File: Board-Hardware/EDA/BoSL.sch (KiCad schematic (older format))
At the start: 56 parts, among them CON1 Micro_SD_Card, CON2 BARREL_JACK, IC1 ATMEGA328-P, IC2 SIM7000, J1 Screw_Terminal_1x06, J2 Screw_Terminal_1x04, J3 Screw_Terminal_1x02, J4 Screw_Terminal_1x08, J5 Screw_Terminal_1x04, J6 RJ45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

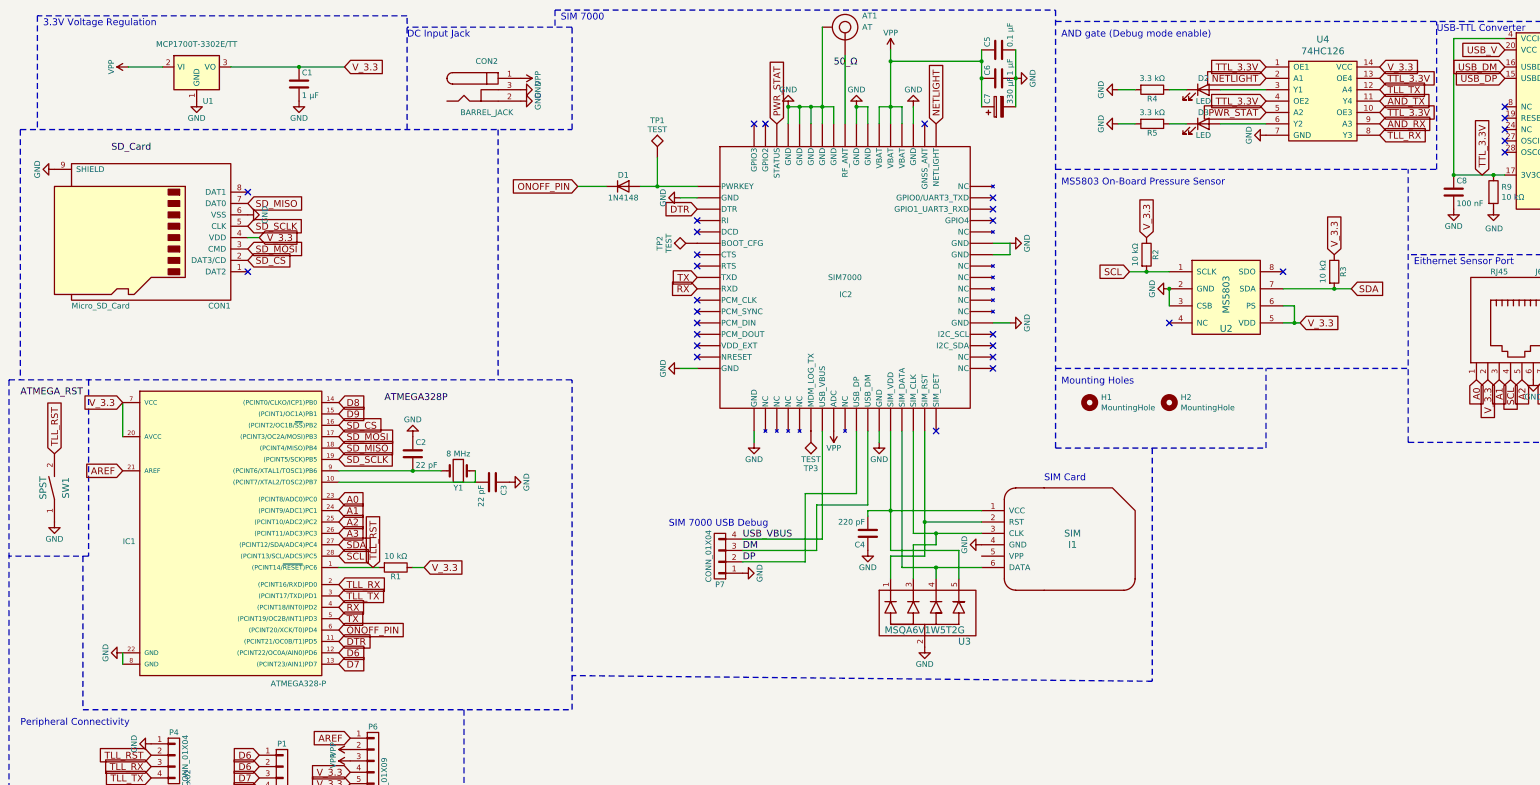
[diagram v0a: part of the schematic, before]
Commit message: renamed bosl GPS to bosl
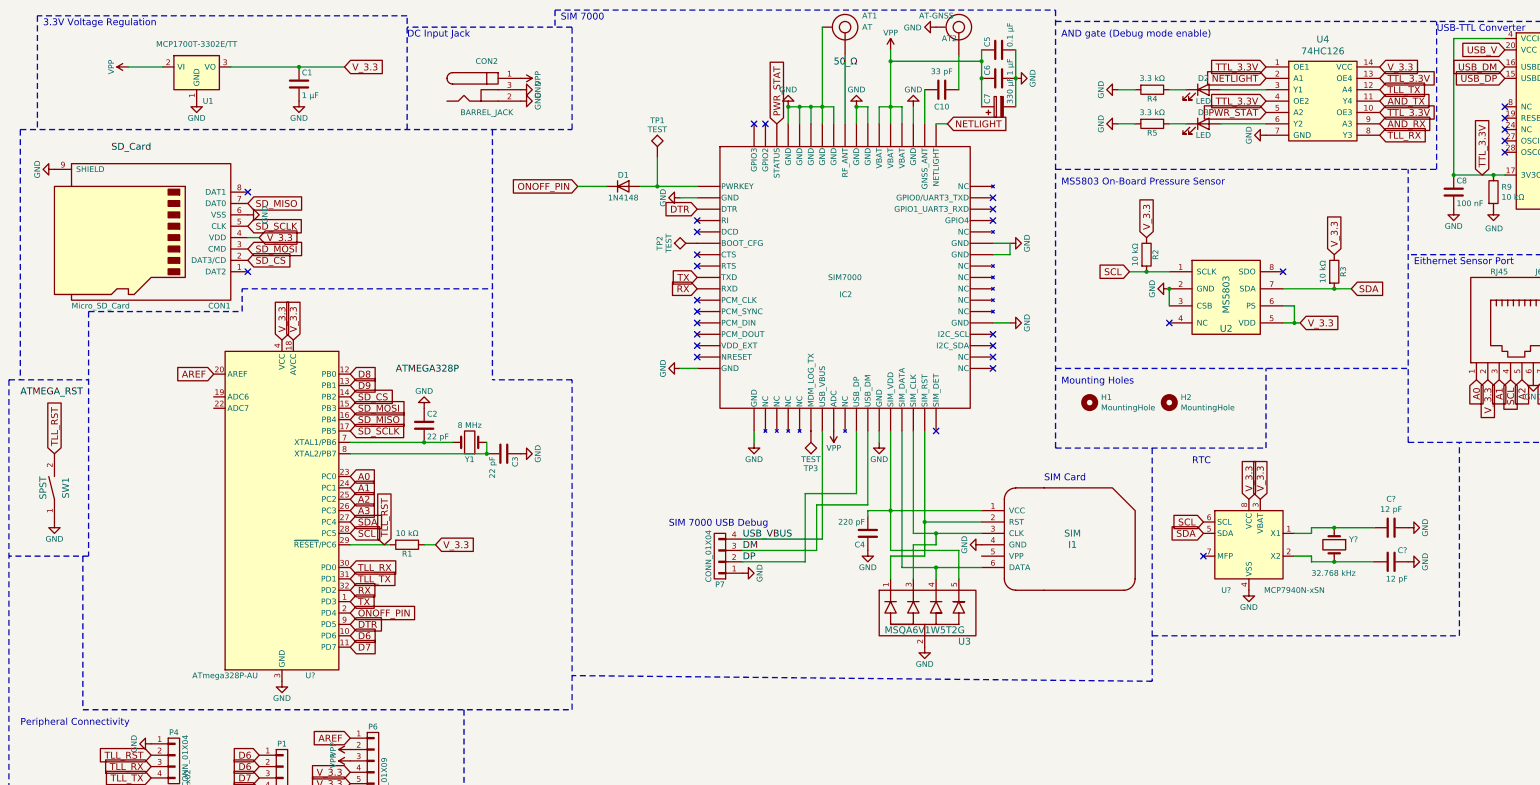
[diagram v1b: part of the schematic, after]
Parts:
- removed IC1: ATMEGA328-P, Housings_DIP:DIP-28_W7.62mm_Socket_LongPads, symbol SIM7000-rescue:ATMEGA328-P-SIM7000-rescue
- added AT2: AT-GNSS, Connectors_Molex:Molex_Microcoaxial_RF, symbol SIM7000-rescue:AT-ant
- added C10: 33 pF, Capacitors_SMD:C_0805_HandSoldering, symbol Device:C
- added C? (x2): 12 pF, Capacitor_SMD:C_0805_2012Metric, symbol Device:C
- added U?: MCP7940N-xSN, symbol Timer:MCP7940N-xSN
- added U?: ATmega328P-AU, Package_QFP:TQFP-32_7x7mm_P0.8mm, symbol MCU_Microchip_ATmega:ATmega328P-AU
- added Y?: 32.768 kHz, Crystal:Crystal_SMD_EuroQuartz_EQ161-2Pin_3.2x1.5mm, symbol Device:Crystal
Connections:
- net A0: now also U?.23 (PC0)
- net A1: now also U?.24 (PC1)
- net A2: now also U?.25 (PC2)
- net A3: now also U?.26 (PC3)
- net AREF: now also U?.20 (AREF)
- net D6: now also U?.10 (PD6)
- net D7: now also U?.11 (PD7)
- net D8: now also U?.12 (PB0)
- net D9: now also U?.13 (PB1)
- net DTR: now also U?.9 (PD5)
- net GND: now also AT2.2, C?.1, C?.1, U?.21 (GND), U?.3 (GND), U?.4 (VSS), U?.5 (GND)
- net ONOFF_PIN: now also U?.2 (PD4)
- net RX: now also U?.32 (PD2)
- net SCL: now also U?.28 (PC5), U?.6 (SCL)
- net SDA: now also U?.27 (PC4), U?.5 (SDA)
- net SD_CS: now also U?.14 (PB2)
- net SD_MISO: now also U?.16 (PB4)
- net SD_MOSI: now also U?.15 (PB3)
- net SD_SCLK: now also U?.17 (PB5)
- net TLL_RST: now also U?.29 (~RESET~/PC6)
- net TLL_RX: now also U?.30 (PD0)
- net TLL_TX: now also U?.31 (PD1)
- net TX: now also U?.1 (PD3)
- net V_3.3: now also U?.18 (AVCC), U?.3 (VBAT), U?.4 (VCC), U?.6 (VCC), U?.8 (VCC)
- net at IC2.53 (GNSS_ANT): now also C10.2
- net at C3.2, Y1.1: now also U?.8 (XTAL2/PB7)
- net at C2.2, Y1.2: now also U?.7 (XTAL1/PB6)
- new net: AT2.1, C10.1
- new net: C?.2, U?.1 (X1), Y?.1
- new net: C?.2, U?.2 (X2), Y?.2
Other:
- note added: "RTC\n"
- moved on the sheet: C2, C3, R1, Y1

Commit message: begun layout of bosl board rev 0.4
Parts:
- U7: renamed from U?; footprint (none) -> Package_SO:SOIC-8_3.9x4.9mm_P1.27mm
- gave numbers to parts that had none: 4
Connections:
- net D6: now also J4.3, P1.5 (P5), P1.6 (P6); no longer J4.1, P1.1 (P1), P1.2 (P2)
- net D7: now also J4.4, P1.7 (P7), P1.8 (P8); no longer J4.2, P1.3 (P3), P1.4 (P4)
- net RX: now also U6.12 (PB0); no longer U6.32 (PD2)
- net TX: now also U6.13 (PB1); no longer U6.1 (PD3)
- removed net D8: J4.3, P1.5 (P5), P1.6 (P6), U6.12 (PB0)
- removed net D9: J4.4, P1.7 (P7), P1.8 (P8), U6.13 (PB1)
- new net D2: J4.1, P1.1 (P1), P1.2 (P2), U6.32 (PD2)
- new net D3: J4.2, P1.3 (P3), P1.4 (P4), U6.1 (PD3)
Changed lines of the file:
@@
 	0    -1   -1   0
 $EndComp
-Text GLabel 3500 3800 2    60   Input ~ 0
-D9
+Text GLabel 3500 5700 2    60   Input ~ 0
+D3
 $Comp
 L power:VPP #PWR04
@@
 Text GLabel 3500 4200 2    60   Input ~ 0
 SD_SCLK
-Text GLabel 3500 5600 2    60   Input ~ 0
+Text GLabel 3500 3700 2    60   Input ~ 0
 RX
-Text GLabel 3500 5700 2    60   Input ~ 0
+Text GLabel 3500 3800 2    60   Input ~ 0
 TX
 Text GLabel 3500 4000 2    60   Input ~ 0
@@
 Text GLabel 3500 6100 2    60   Input ~ 0
 D7
-Text GLabel 3500 3700 2    60   Input ~ 0
-D8
+Text GLabel 3500 5600 2    60   Input ~ 0
+D2
 Text GLabel 2300 3700 0    60   Input ~ 0
 AREF
@@
 Text GLabel 2800 9400 0    60   Input ~ 0
 SD_CS
+Text GLabel 2800 10000 0    60   Input ~ 0
+D3
+Text GLabel 2800 10200 0    60   Input ~ 0
+D2
 Text GLabel 2800 9600 0    60   Input ~ 0
-D9
-Text GLabel 2800 9800 0    60   Input ~ 0
-D8
-Text GLabel 2800 10000 0    60   Input ~ 0
 D7
 $Comp
@@
 	-1   0    0    1
 $EndComp
-Text GLabel 2800 10200 0    60   Input ~ 0
+Text GLabel 2800 9800 0    60   Input ~ 0
 D6
 $Comp
@@
 	1    0    0    -1
 $EndComp
+Text GLabel 2700 7450 0    60   Input ~ 0
+D6
+Text GLabel 2700 7550 0    60   Input ~ 0
+D6
+Text GLabel 2700 7650 0    60   Input ~ 0
+D7
+Text GLabel 2700 7750 0    60   Input ~ 0
+D7
 Text GLabel 2700 7050 0    60   Input ~ 0
-D6
+D2
 Text GLabel 2700 7150 0    60   Input ~ 0
-D6
+D2
 Text GLabel 2700 7250 0    60   Input ~ 0
-D7
+D3
 Text GLabel 2700 7350 0    60   Input ~ 0
-D7
-Text GLabel 2700 7450 0    60   Input ~ 0
-D8
-Text GLabel 2700 7550 0    60   Input ~ 0
-D8
-Text GLabel 2700 7650 0    60   Input ~ 0
-D9
-Text GLabel 2700 7750 0    60   Input ~ 0
-D9
+D3
 Text GLabel 2700 7850 0    60   Input ~ 0
 SD_CS
@@
 $EndComp
 $Comp
-L Timer:MCP7940N-xSN U?
+L Timer:MCP7940N-xSN U7
 U 1 1 5E98247E
 P 11400 5200
-F 0 "U?" H 11200 4800 50  0000 C CNN
+F 0 "U7" H 11200 4800 50  0000 C CNN
 F 1 "MCP7940N-xSN" H 11800 4800 50  0000 C CNN
-F 2 "" H 11400 5200 50  0001 C CNN
+F 2 "Package_SO:SOIC-8_3.9x4.9mm_P1.27mm" H 11400 5200 50  0001 C CNN
 F 3 "http://ww1.microchip.com/downloads/en/DeviceDoc/20005010F.pdf" H 11400 5200 50  0001 C CNN
 	1    11400 5200
@@
 V_3.3
 $Comp
-L power:GND #PWR?
+L power:GND #PWR022
 U 1 1 5E98293F
 P 11400 5600
-F 0 "#PWR?" H 11400 5350 50  0001 C CNN
+F 0 "#PWR022" H 11400 5350 50  0001 C CNN
 F 1 "GND" H 11400 5450 50  0000 C CNN
 F 2 "" H 11400 5600 50  0000 C CNN
@@
 $EndComp
 $Comp
-L Device:Crystal Y?
+L Device:Crystal Y2
 U 1 1 5E983AB6
 P 12150 5200
-F 0 "Y?" V 12104 5331 50  0000 L CNN
+F 0 "Y2" V 12104 5331 50  0000 L CNN
 F 1 " 32.768 kHz" V 12400 5000 50  0000 L CNN
 F 2 "Crystal:Crystal_SMD_EuroQuartz_EQ161-2Pin_3.2x1.5mm" H 12150 5200 50  0001 C CNN
@@
 $EndComp
 $Comp
-L Device:C C?
+L Device:C C11
 U 1 1 5E983D64
 P 12650 5050
-F 0 "C?" V 12398 5050 50  0000 C CNN
+F 0 "C11" V 12398 5050 50  0000 C CNN
 F 1 "12 pF" V 12489 5050 50  0000 C CNN
 F 2 "Capacitor_SMD:C_0805_2012Metric" H 12688 4900 50  0001 C CNN
@@
 $EndComp
 $Comp
-L Device:C C?
+L Device:C C12
 U 1 1 5E984B65
 P 12650 5350
-F 0 "C?" V 12550 5450 50  0000 C CNN
+F 0 "C12" V 12550 5500 50  0000 C CNN
 F 1 "12 pF" V 12800 5400 50  0000 C CNN
 F 2 "Capacitor_SMD:C_0805_2012Metric" H 12688 5200 50  0001 C CNN
@@
 	12150 5350 11950 5350
 $Comp
-L power:GND #PWR?
+L power:GND #PWR053
 U 1 1 5E990792
 P 12800 5050
-F 0 "#PWR?" H 12800 4800 50  0001 C CNN
+F 0 "#PWR053" H 12800 4800 50  0001 C CNN
 F 1 "GND" H 12800 4900 50  0000 C CNN
 F 2 "" H 12800 5050 50  0000 C CNN
@@
 $EndComp
 $Comp
-L power:GND #PWR?
+L power:GND #PWR054
 U 1 1 5E990C8E
 P 12800 5350
-F 0 "#PWR?" H 12800 5100 50  0001 C CNN
+F 0 "#PWR054" H 12800 5100 50  0001 C CNN
 F 1 "GND" H 12800 5200 50  0000 C CNN
 F 2 "" H 12800 5350 50  0000 C CNN
@@
 RTC\n
 $Comp
-L MCU_Microchip_ATmega:ATmega328P-AU U?
+L MCU_Microchip_ATmega:ATmega328P-AU U6
 U 1 1 5E998630
 P 2900 4900
-F 0 "U?" H 3150 3450 50  0000 C CNN
+F 0 "U6" H 3150 3450 50  0000 C CNN
 F 1 "ATmega328P-AU" H 2400 3450 50  0000 C CNN
 F 2 "Package_QFP:TQFP-32_7x7mm_P0.8mm" H 2900 4900 50  0001 C CIN

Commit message: finished bosl board rev0.4 layout
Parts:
- C1, C6: footprint Capacitors_SMD:C_1206_HandSoldering -> Capacitor_SMD:C_1206_3216Metric
- C10, C2, C3, C4, C5, C8, C9: footprint Capacitors_SMD:C_0805_HandSoldering -> Capacitor_SMD:C_0805_2012Metric
- D2, D3, D4, D5, D6: footprint LEDs:LED_0805_HandSoldering -> LED_SMD:LED_0805_2012Metric
- R1, R2, R3, R4, R5, R6, R7, R8, R9: footprint Resistors_SMD:R_0805_HandSoldering -> Resistor_SMD:R_0805_2012Metric
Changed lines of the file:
@@
 F 0 "R1" V 4080 5200 50  0000 C CNN
 F 1 "10 kΩ" V 3900 5200 50  0000 C CNN
-F 2 "Resistors_SMD:R_0805_HandSoldering" V 3930 5200 50  0001 C CNN
+F 2 "Resistor_SMD:R_0805_2012Metric" V 3930 5200 50  0001 C CNN
 F 3 "" H 4000 5200 50  0000 C CNN
 	1    4000 5200
@@
 F 0 "C2" H 4175 4250 50  0000 L CNN
 F 1 "22 pF" H 4175 4050 50  0000 L CNN
-F 2 "Capacitors_SMD:C_0805_HandSoldering" H 4188 4000 50  0001 C CNN
+F 2 "Capacitor_SMD:C_0805_2012Metric" H 4188 4000 50  0001 C CNN
 F 3 "" H 4150 4150 50  0000 C CNN
 	1    4150 4150
@@
 F 0 "C3" H 4875 4500 50  0000 L CNN
 F 1 "22 pF" H 4875 4300 50  0000 L CNN
-F 2 "Capacitors_SMD:C_0805_HandSoldering" H 4888 4250 50  0001 C CNN
+F 2 "Capacitor_SMD:C_0805_2012Metric" H 4888 4250 50  0001 C CNN
 F 3 "" H 4850 4400 50  0000 C CNN
 	1    4850 4400
@@
 F 0 "C4" H 8075 5200 50  0000 L CNN
 F 1 "220 pF" H 8075 5000 50  0000 L CNN
-F 2 "Capacitors_SMD:C_0805_HandSoldering" H 8088 4950 50  0001 C CNN
+F 2 "Capacitor_SMD:C_0805_2012Metric" H 8088 4950 50  0001 C CNN
 F 3 "" H 8050 5100 50  0000 C CNN
 	1    8050 5100
@@
 F 0 "C1" H 3075 1250 50  0000 L CNN
 F 1 "1 μF" H 3075 1050 50  0000 L CNN
-F 2 "Capacitors_SMD:C_1206_HandSoldering" H 3088 1000 50  0001 C CNN
+F 2 "Capacitor_SMD:C_1206_3216Metric" H 3088 1000 50  0001 C CNN
 F 3 "" H 3050 1150 50  0000 C CNN
 	1    3050 1150
@@
 F 0 "C5" H 9225 950 50  0000 L CNN
 F 1 "0.1 μF" H 9225 750 50  0000 L CNN
-F 2 "Capacitors_SMD:C_0805_HandSoldering" H 9238 700 50  0001 C CNN
+F 2 "Capacitor_SMD:C_0805_2012Metric" H 9238 700 50  0001 C CNN
 F 3 "" H 9200 850 50  0000 C CNN
 	1    9200 850
@@
 F 0 "C6" H 9225 1200 50  0000 L CNN
 F 1 "1 μF" H 9225 1000 50  0000 L CNN
-F 2 "Capacitors_SMD:C_1206_HandSoldering" H 9238 950 50  0001 C CNN
+F 2 "Capacitor_SMD:C_1206_3216Metric" H 9238 950 50  0001 C CNN
 F 3 "" H 9200 1100 50  0000 C CNN
 	1    9200 1100
@@
 F 0 "C8" H 13225 2200 50  0000 L CNN
 F 1 "100 nF" H 13225 2000 50  0000 L CNN
-F 2 "Capacitors_SMD:C_0805_HandSoldering" H 13238 1950 50  0001 C CNN
+F 2 "Capacitor_SMD:C_0805_2012Metric" H 13238 1950 50  0001 C CNN
 F 3 "" H 13200 2100 50  0000 C CNN
 	1    13200 2100
@@
 F 0 "C9" H 15125 1250 50  0000 L CNN
 F 1 "100 nF" H 15125 1050 50  0000 L CNN
-F 2 "Capacitors_SMD:C_0805_HandSoldering" H 15138 1000 50  0001 C CNN
+F 2 "Capacitor_SMD:C_0805_2012Metric" H 15138 1000 50  0001 C CNN
 F 3 "" H 15100 1150 50  0000 C CNN
 	1    15100 1150
@@
 F 0 "D5" H 15450 1650 50  0000 C CNN
 F 1 "LED" H 15450 1450 50  0000 C CNN
-F 2 "LEDs:LED_0805_HandSoldering" H 15450 1550 50  0001 C CNN
+F 2 "LED_SMD:LED_0805_2012Metric" H 15450 1550 50  0001 C CNN
 F 3 "" H 15450 1550 50  0000 C CNN
 	1    15450 1550
@@
 F 0 "R7" V 15180 1550 50  0000 C CNN
 F 1 "3.3 kΩ" V 15000 1550 50  0000 C CNN
-F 2 "Resistors_SMD:R_0805_HandSoldering" V 15030 1550 50  0001 C CNN
+F 2 "Resistor_SMD:R_0805_2012Metric" V 15030 1550 50  0001 C CNN
 F 3 "" H 15100 1550 50  0000 C CNN
 	1    15100 1550
@@
 F 0 "D4" H 15750 3700 50  0000 C CNN
 F 1 "LED" H 15750 3500 50  0000 C CNN
-F 2 "LEDs:LED_0805_HandSoldering" H 15750 3600 50  0001 C CNN
+F 2 "LED_SMD:LED_0805_2012Metric" H 15750 3600 50  0001 C CNN
 F 3 "" H 15750 3600 50  0000 C CNN
 	1    15750 3600
@@
 F 0 "R6" V 15830 3150 50  0000 C CNN
 F 1 "3.3 kΩ" V 15650 3150 50  0000 C CNN
-F 2 "Resistors_SMD:R_0805_HandSoldering" V 15680 3150 50  0001 C CNN
+F 2 "Resistor_SMD:R_0805_2012Metric" V 15680 3150 50  0001 C CNN
 F 3 "" H 15750 3150 50  0000 C CNN
 	1    15750 3150
@@
 F 0 "D3" H 11000 1600 50  0000 C CNN
 F 1 "LED" H 11000 1400 50  0000 C CNN
-F 2 "LEDs:LED_0805_HandSoldering" H 11000 1500 50  0001 C CNN
+F 2 "LED_SMD:LED_0805_2012Metric" H 11000 1500 50  0001 C CNN
 F 3 "" H 11000 1500 50  0000 C CNN
 	1    11000 1500
@@
 F 0 "R5" V 10630 1500 50  0000 C CNN
 F 1 "3.3 kΩ" V 10450 1500 50  0000 C CNN
-F 2 "Resistors_SMD:R_0805_HandSoldering" V 10480 1500 50  0001 C CNN
+F 2 "Resistor_SMD:R_0805_2012Metric" V 10480 1500 50  0001 C CNN
 F 3 "" H 10550 1500 50  0000 C CNN
 	1    10550 1500
@@
 F 0 "D2" H 11000 1300 50  0000 C CNN
 F 1 "LED" H 11000 1100 50  0000 C CNN
-F 2 "LEDs:LED_0805_HandSoldering" H 11000 1200 50  0001 C CNN
+F 2 "LED_SMD:LED_0805_2012Metric" H 11000 1200 50  0001 C CNN
 F 3 "" H 11000 1200 50  0000 C CNN
 	1    11000 1200
@@
 F 0 "R4" V 10630 1200 50  0000 C CNN
 F 1 "3.3 kΩ" V 10450 1200 50  0000 C CNN
-F 2 "Resistors_SMD:R_0805_HandSoldering" V 10480 1200 50  0001 C CNN
+F 2 "Resistor_SMD:R_0805_2012Metric" V 10480 1200 50  0001 C CNN
 F 3 "" H 10550 1200 50  0000 C CNN
 	1    10550 1200
@@
 F 0 "D6" H 15450 1750 50  0000 C CNN
 F 1 "LED" H 15450 1550 50  0000 C CNN
-F 2 "LEDs:LED_0805_HandSoldering" H 15450 1650 50  0001 C CNN
+F 2 "LED_SMD:LED_0805_2012Metric" H 15450 1650 50  0001 C CNN
 F 3 "" H 15450 1650 50  0000 C CNN
 	1    15450 1650
@@
 F 0 "R8" V 15180 1650 50  0000 C CNN
 F 1 "3.3 kΩ" V 15000 1650 50  0000 C CNN
-F 2 "Resistors_SMD:R_0805_HandSoldering" V 15030 1650 50  0001 C CNN
+F 2 "Resistor_SMD:R_0805_2012Metric" V 15030 1650 50  0001 C CNN
 F 3 "" H 15100 1650 50  0000 C CNN
 	1    15100 1650
@@
 F 0 "R3" V 12230 2800 50  0000 C CNN
 F 1 "10 kΩ" V 12050 2800 50  0000 C CNN
-F 2 "Resistors_SMD:R_0805_HandSoldering" V 12080 2800 50  0001 C CNN
+F 2 "Resistor_SMD:R_0805_2012Metric" V 12080 2800 50  0001 C CNN
 F 3 "" H 12150 2800 50  0000 C CNN
 	1    12150 2800
@@
 F 0 "R2" V 10580 2650 50  0000 C CNN
 F 1 "10 kΩ" V 10400 2650 50  0000 C CNN
-F 2 "Resistors_SMD:R_0805_HandSoldering" V 10430 2650 50  0001 C CNN
+F 2 "Resistor_SMD:R_0805_2012Metric" V 10430 2650 50  0001 C CNN
 F 3 "" H 10500 2650 50  0000 C CNN
 	1    10500 2650
@@
 F 0 "R9" H 13620 2145 50  0000 L CNN
 F 1 "10 kΩ" H 13620 2056 50  0000 L CNN
-F 2 "Resistors_SMD:R_0805_HandSoldering" V 13480 2100 50  0001 C CNN
+F 2 "Resistor_SMD:R_0805_2012Metric" V 13480 2100 50  0001 C CNN
 F 3 "~" H 13550 2100 50  0001 C CNN
 	1    13550 2100
@@
 F 0 "C10" V 8850 1200 50  0000 C CNN
 F 1 "33 pF" V 8540 1200 50  0000 C CNN
-F 2 "Capacitors_SMD:C_0805_HandSoldering" H 8738 1050 50  0001 C CNN
+F 2 "Capacitor_SMD:C_0805_2012Metric" H 8738 1050 50  0001 C CNN
 F 3 "~" H 8700 1200 50  0001 C CNN
 	1    8700 1200
